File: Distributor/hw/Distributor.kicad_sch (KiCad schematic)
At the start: 61 parts, among them J1 Conn_01x04, J100 Conn_01x03, J101 Conn_01x03, J102 Conn_01x03, J103 Conn_01x03, J104 Conn_01x03, J105 Conn_01x03, J106 Conn_01x03, J107 Conn_01x03, J108 Conn_01x03, J109 Conn_01x03, J110 Conn_01x03, J111 Conn_01x03, J112 Conn_01x03, J113 Conn_01x03, J114 Conn_01x03, J115 Conn_01x03, J116 Conn_01x03, J117 Conn_01x03, J118 Conn_01x03, J119 Conn_01x03, J120 Conn_01x03, J121 Conn_01x03, J122 Conn_01x03, J123 Conn_01x03, J124 Conn_01x03, J125 Conn_01x03, J126 Conn_01x03, J127 Conn_01x03, J128 Conn_01x03, J129 Conn_01x03, J130 Conn_01x03, J131 Conn_01x03, J2 Conn_01x06_MountingPin, J3 Conn_01x02, J4 Conn_01x02, J5 Conn_01x02, J6 Conn_01x02, U1 SPX3819M5-L-3-3, U2 STM32G030C8Tx, U3 SN74AHCT245PWR, U4 SN74AHCT245PWR, U5 SN74AHCT245PWR, U6 SN74AHCT245PWR

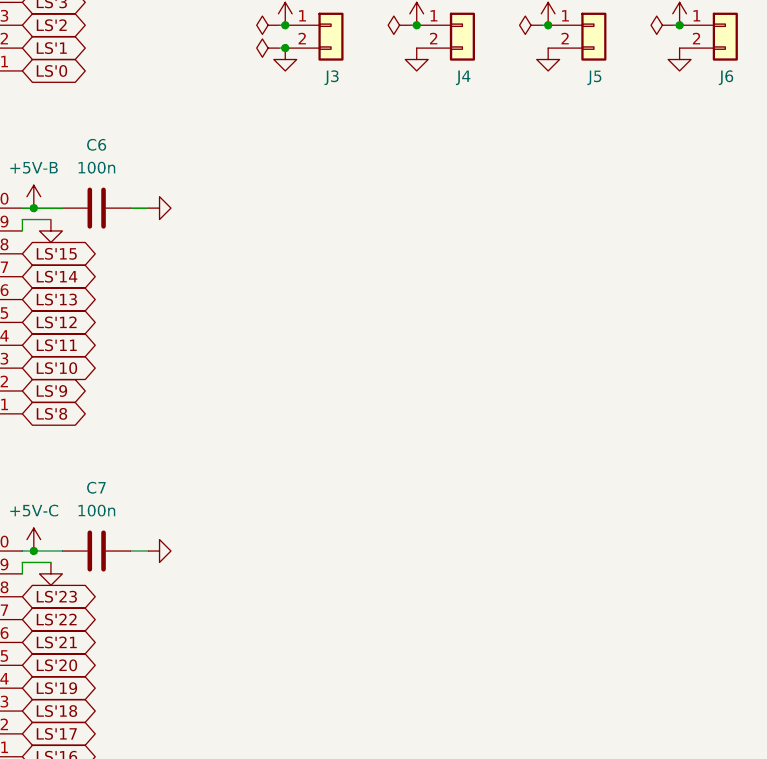
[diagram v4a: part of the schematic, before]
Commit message: Revise distributor board; submit for fab
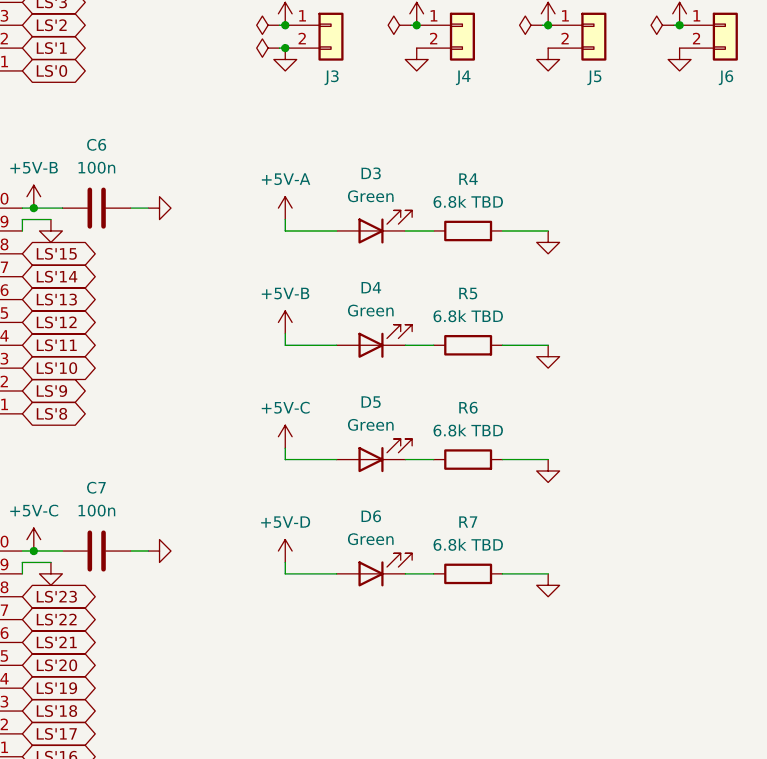
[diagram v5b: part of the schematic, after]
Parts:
- added D3, D4, D5, D6: Green, LED_SMD:LED_0603_1608Metric, symbol Device:LED
- added R4, R5, R6, R7: 6.8k TBD, Resistor_SMD:R_0603_1608Metric, symbol Device:R
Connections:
- net +5V-A: now also D3.2 (A)
- net +5V-B: now also D4.2 (A)
- net +5V-C: now also D5.2 (A)
- net +5V-D: now also D6.2 (A)
- net GND: now also R4.2, R5.2, R6.2, R7.2
- new net: D6.1 (K), R7.1
- new net: D4.1 (K), R5.1
- new net: D3.1 (K), R4.1
- new net: D5.1 (K), R6.1

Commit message: I hate layout
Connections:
- net LS16: now also U2.34 (PA12/PA10); no longer U2.27 (PB15)
- net LS17: now also U2.33 (PA11/PA9); no longer U2.28 (PA8)
- net LS18: now also U2.32 (PA10/NC); no longer U2.29 (PA9/NC)
- net LS19: now also U2.31 (PC7); no longer U2.30 (PC6)
- net LS20: now also U2.30 (PC6); no longer U2.31 (PC7)
- net LS21: now also U2.29 (PA9/NC); no longer U2.32 (PA10/NC)
- net LS22: now also U2.28 (PA8); no longer U2.33 (PA11/PA9)
- net LS23: now also U2.27 (PB15); no longer U2.34 (PA12/PA10)
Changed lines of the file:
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@@
     )
   )
-  (global_label "LS17" (shape bidirectional) (at 127 55.245 0) (fields_autoplaced)
-    (effects (font (size 1.27 1.27)) (justify left))
-    (property "Intersheetrefs" "${INTERSHEET_REFS}" (at 134.5436 55.245 0)
+  (global_label "LS22" (shape bidirectional) (at 127 55.245 0) (fields_autoplaced)
+    (effects (font (size 1.27 1.27)) (justify left))
+    (property "Intersheetrefs" "${INTERSHEET_REFS}" (at 135.7531 55.245 0)
       (effects (font (size 1.27 1.27)) (justify left) hide)
     )
@@
     )
   )
-  (global_label "LS23" (shape bidirectional) (at 127 65.405 0) (fields_autoplaced)
-    (effects (font (size 1.27 1.27)) (justify left))
-    (property "Intersheetrefs" "${INTERSHEET_REFS}" (at 134.5436 65.405 0)
+  (global_label "LS16" (shape bidirectional) (at 127 65.405 0) (fields_autoplaced)
+    (effects (font (size 1.27 1.27)) (justify left))
+    (property "Intersheetrefs" "${INTERSHEET_REFS}" (at 135.7531 65.405 0)
       (effects (font (size 1.27 1.27)) (justify left) hide)
     )
@@
     )
   )
-  (global_label "LS18" (shape bidirectional) (at 127 57.785 0) (fields_autoplaced)
-    (effects (font (size 1.27 1.27)) (justify left))
-    (property "Intersheetrefs" "${INTERSHEET_REFS}" (at 134.5436 57.785 0)
+  (global_label "LS21" (shape bidirectional) (at 127 57.785 0) (fields_autoplaced)
+    (effects (font (size 1.27 1.27)) (justify left))
+    (property "Intersheetrefs" "${INTERSHEET_REFS}" (at 135.7531 57.785 0)
       (effects (font (size 1.27 1.27)) (justify left) hide)
     )
@@
     )
   )
-  (global_label "LS19" (shape bidirectional) (at 96.52 65.405 180) (fields_autoplaced)
-    (effects (font (size 1.27 1.27)) (justify right))
-    (property "Intersheetrefs" "${INTERSHEET_REFS}" (at 88.9764 65.405 0)
+  (global_label "LS20" (shape bidirectional) (at 96.52 65.405 180) (fields_autoplaced)
+    (effects (font (size 1.27 1.27)) (justify right))
+    (property "Intersheetrefs" "${INTERSHEET_REFS}" (at 87.7669 65.405 0)
       (effects (font (size 1.27 1.27)) (justify right) hide)
     )
@@
     )
   )
-  (global_label "LS22" (shape bidirectional) (at 127 62.865 0) (fields_autoplaced)
-    (effects (font (size 1.27 1.27)) (justify left))
-    (property "Intersheetrefs" "${INTERSHEET_REFS}" (at 134.5436 62.865 0)
+  (global_label "LS17" (shape bidirectional) (at 127 62.865 0) (fields_autoplaced)
+    (effects (font (size 1.27 1.27)) (justify left))
+    (property "Intersheetrefs" "${INTERSHEET_REFS}" (at 135.7531 62.865 0)
       (effects (font (size 1.27 1.27)) (justify left) hide)
     )
@@
     )
   )
-  (global_label "LS20" (shape bidirectional) (at 96.52 67.945 180) (fields_autoplaced)
-    (effects (font (size 1.27 1.27)) (justify right))
-    (property "Intersheetrefs" "${INTERSHEET_REFS}" (at 88.9764 67.945 0)
+  (global_label "LS19" (shape bidirectional) (at 96.52 67.945 180) (fields_autoplaced)
+    (effects (font (size 1.27 1.27)) (justify right))
+    (property "Intersheetrefs" "${INTERSHEET_REFS}" (at 87.7669 67.945 0)
       (effects (font (size 1.27 1.27)) (justify right) hide)
     )
@@
     )
   )
-  (global_label "LS21" (shape bidirectional) (at 127 60.325 0) (fields_autoplaced)
-    (effects (font (size 1.27 1.27)) (justify left))
-    (property "Intersheetrefs" "${INTERSHEET_REFS}" (at 134.5436 60.325 0)
+  (global_label "LS18" (shape bidirectional) (at 127 60.325 0) (fields_autoplaced)
+    (effects (font (size 1.27 1.27)) (justify left))
+    (property "Intersheetrefs" "${INTERSHEET_REFS}" (at 135.7531 60.325 0)
       (effects (font (size 1.27 1.27)) (justify left) hide)
     )
@@
     )
   )
-  (global_label "LS16" (shape bidirectional) (at 127 116.205 0) (fields_autoplaced)
-    (effects (font (size 1.27 1.27)) (justify left))
-    (property "Intersheetrefs" "${INTERSHEET_REFS}" (at 134.5436 116.205 0)
-      (effects (font (size 1.27 1.27)) (justify left) hide)
-    )
+  (global_label "LS23" (shape bidirectional) (at 127 116.205 0) (fields_autoplaced)
+    (effects (font (size 1.27 1.27)) (justify left))
+    (property "Intersheetrefs" "${INTERSHEET_REFS}" (at 135.7531 116.205 0)
+      (effects (font (size 1.27 1.27)) (justify left) hide)
+    )

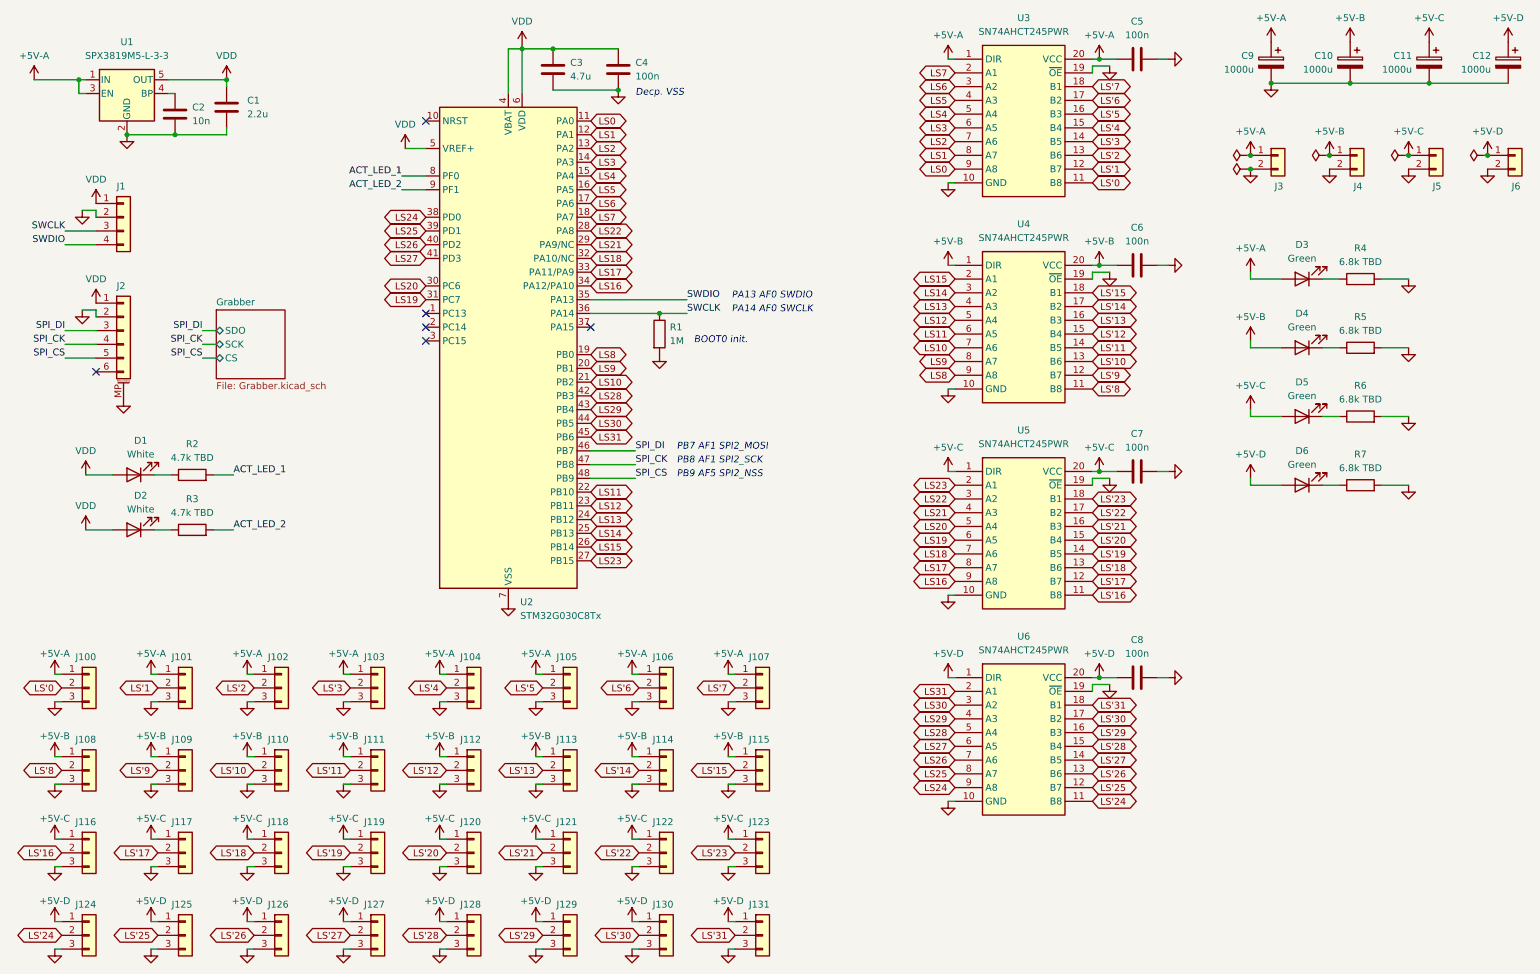
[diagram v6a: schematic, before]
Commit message: Update EDA document with actual values in assembly
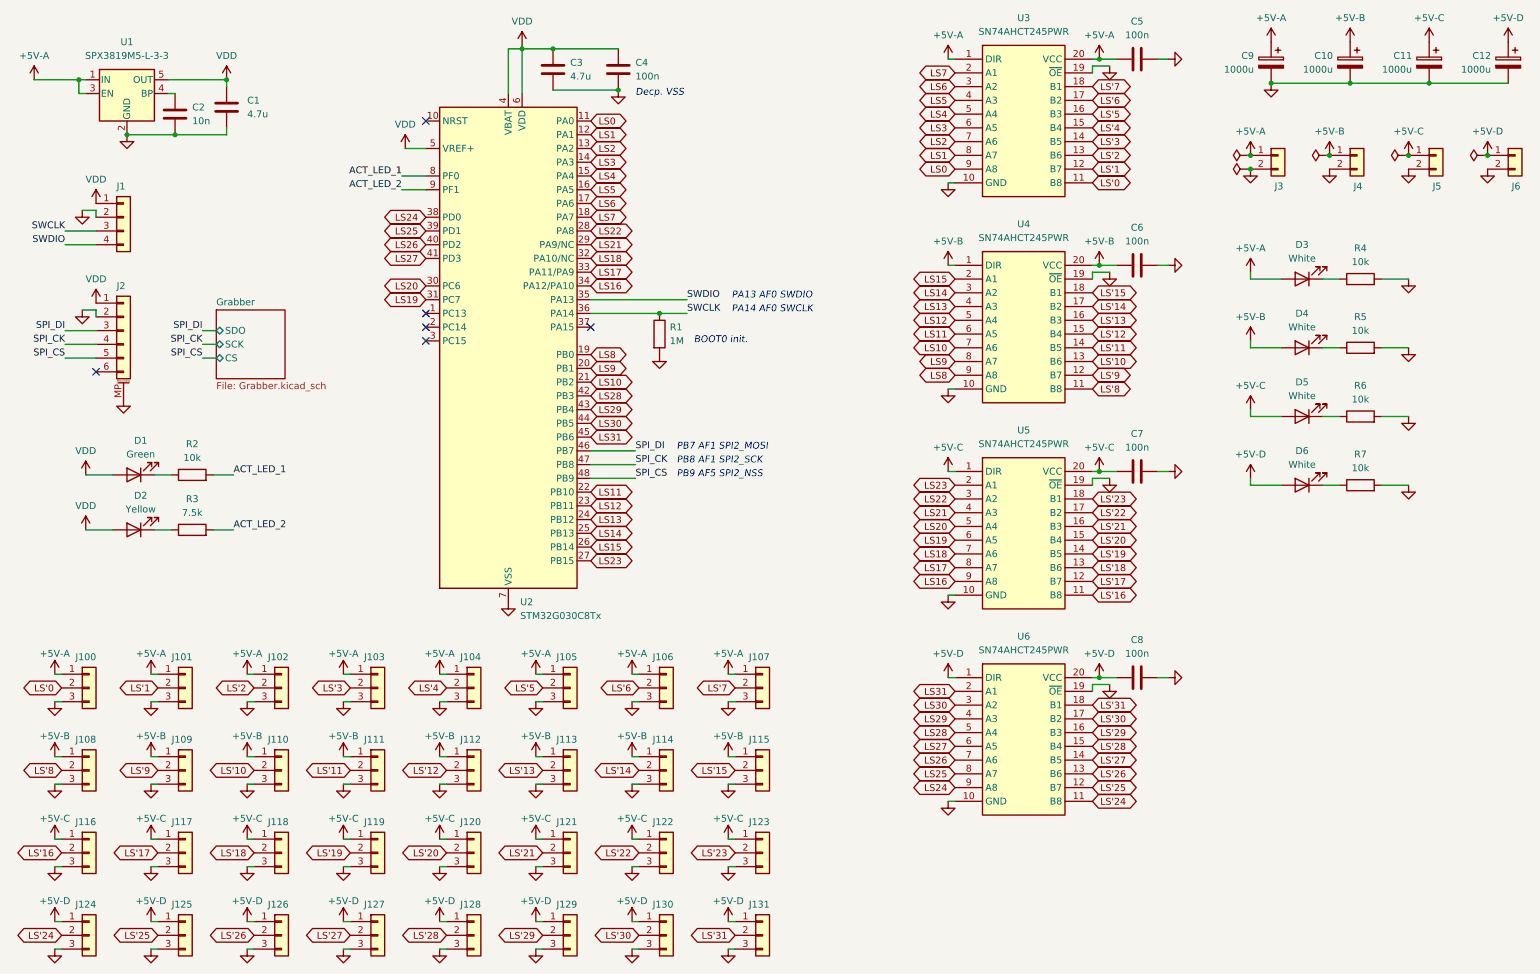
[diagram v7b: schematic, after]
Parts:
- C1: value 2.2u -> 4.7u
- D1: value White -> Green
- D2: value White -> Yellow
- D3, D4, D5, D6: value Green -> White
- R2: value 4.7k TBD -> 10k
- R3: value 4.7k TBD -> 7.5k
- R4, R5, R6, R7: value 6.8k TBD -> 10k
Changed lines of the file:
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@@
       (effects (font (size 1.27 1.27)))
     )
-    (property "Value" "Green" (at 258.445 98.425 0)
+    (property "Value" "White" (at 258.445 98.425 0)
       (effects (font (size 1.27 1.27)))
     )
@@
       (effects (font (size 1.27 1.27)))
     )
-    (property "Value" "4.7k TBD" (at 53.34 107.315 90)
+    (property "Value" "7.5k" (at 53.34 107.315 90)
       (effects (font (size 1.27 1.27)))
     )
@@
       (effects (font (size 1.27 1.27)))
     )
-    (property "Value" "Green" (at 258.445 73.025 0)
+    (property "Value" "White" (at 258.445 73.025 0)
       (effects (font (size 1.27 1.27)))
     )
@@
       (effects (font (size 1.27 1.27)))
     )
-    (property "Value" "6.8k TBD" (at 269.24 99.06 90)
+    (property "Value" "10k" (at 269.24 99.06 90)
       (effects (font (size 1.27 1.27)))
     )
@@
       (effects (font (size 1.27 1.27)))
     )
-    (property "Value" "Green" (at 258.445 60.325 0)
+    (property "Value" "White" (at 258.445 60.325 0)
       (effects (font (size 1.27 1.27)))
     )
@@
       (effects (font (size 1.27 1.27)))
     )
-    (property "Value" "6.8k TBD" (at 269.24 86.36 90)
+    (property "Value" "10k" (at 269.24 86.36 90)
       (effects (font (size 1.27 1.27)))
     )
@@
       (effects (font (size 1.27 1.27)))
     )
-    (property "Value" "White" (at 43.815 96.52 0)
+    (property "Value" "Green" (at 43.815 96.52 0)
       (effects (font (size 1.27 1.27)))
     )
@@
       (effects (font (size 1.27 1.27)))
     )
-    (property "Value" "Green" (at 258.445 85.725 0)
+    (property "Value" "White" (at 258.445 85.725 0)
       (effects (font (size 1.27 1.27)))
     )
@@
       (effects (font (size 1.27 1.27)))
     )
-    (property "Value" "6.8k TBD" (at 269.24 60.96 90)
+    (property "Value" "10k" (at 269.24 60.96 90)
       (effects (font (size 1.27 1.27)))
     )
@@
       (effects (font (size 1.27 1.27)))
     )
-    (property "Value" "White" (at 43.815 106.68 0)
+    (property "Value" "Yellow" (at 43.815 106.68 0)
       (effects (font (size 1.27 1.27)))
     )
@@
       (effects (font (size 1.27 1.27)))
     )
-    (property "Value" "4.7k TBD" (at 53.34 97.155 90)
+    (property "Value" "10k" (at 53.34 97.155 90)
       (effects (font (size 1.27 1.27)))
     )
@@
       (effects (font (size 1.27 1.27)))
     )
-    (property "Value" "6.8k TBD" (at 269.24 73.66 90)
+    (property "Value" "10k" (at 269.24 73.66 90)
       (effects (font (size 1.27 1.27)))
     )
@@
       (effects (font (size 1.27 1.27)) (justify left))
     )
-    (property "Value" "2.2u" (at 63.5 33.655 0)
+    (property "Value" "4.7u" (at 63.5 33.655 0)
       (effects (font (size 1.27 1.27)) (justify left))
     )
